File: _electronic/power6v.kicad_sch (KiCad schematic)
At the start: 19 parts

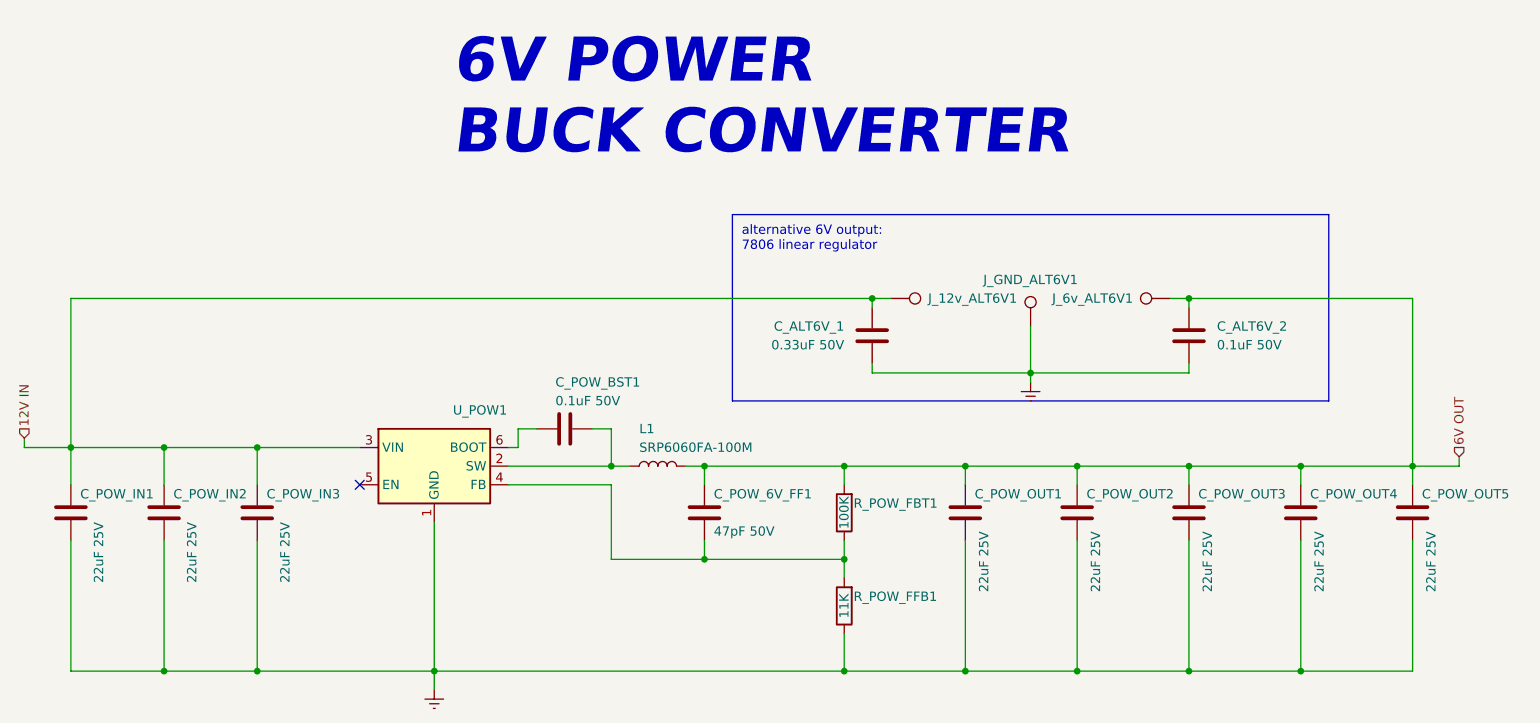
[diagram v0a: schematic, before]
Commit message: BETA first upload
nothing major done here:
* updated KiCAD files to v9
* removed alternative 6v feed-in. The proposed buck converter is fine.
* added to all components LCSC component IDs. With this, exporting the project as gerber files also automatically creates correct BOM for JLCPCB manufacturing
*
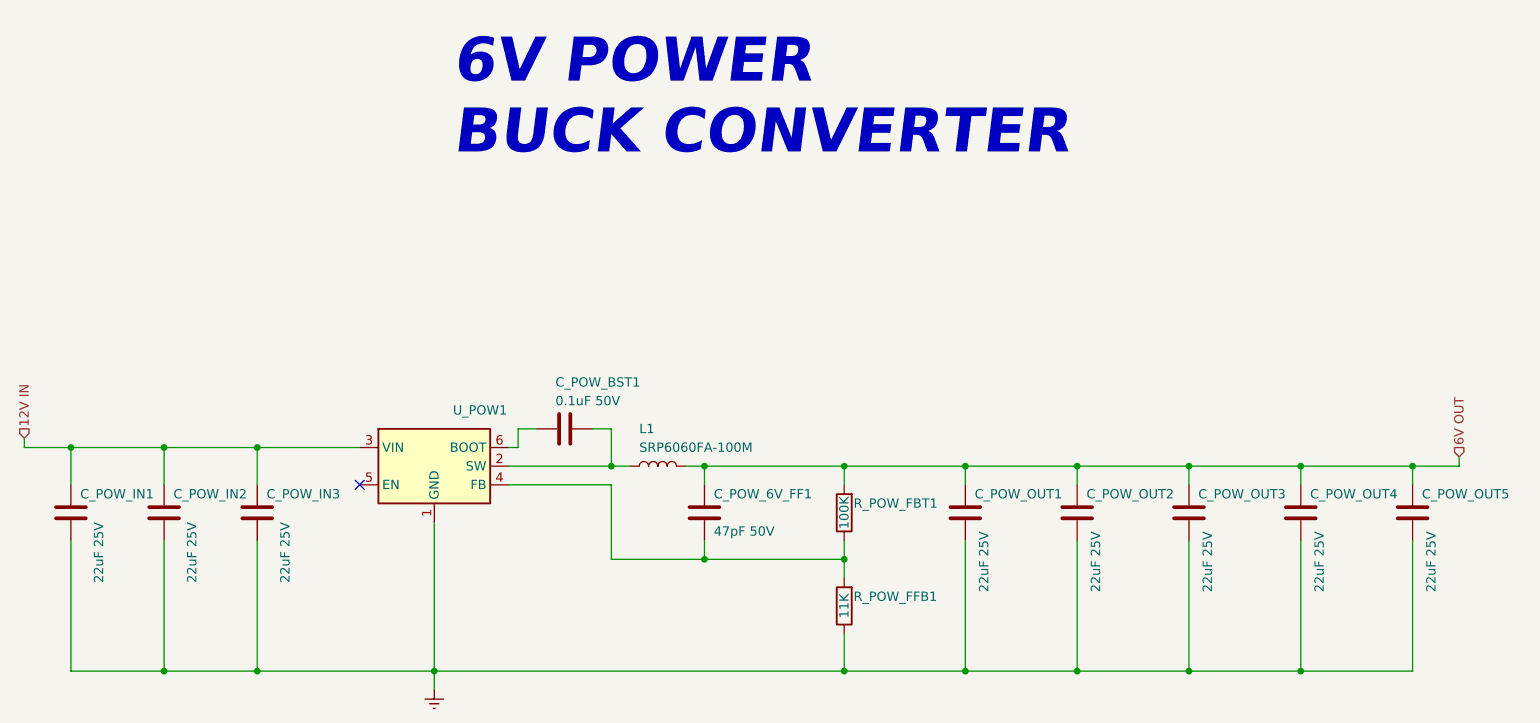
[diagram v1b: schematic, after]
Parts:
- removed C_ALT6V_1: 0.33uF 50V, Capacitor_SMD:C_0603_1608Metric_Pad1.08x0.95mm_HandSolder, symbol Device:C
- removed C_ALT6V_2: 0.1uF 50V, Capacitor_SMD:C_0603_1608Metric_Pad1.08x0.95mm_HandSolder, symbol Device:C
- removed J_12v_ALT6V1, J_6v_ALT6V1, J_GND_ALT6V1: TestPoint, TestPoint:TestPoint_Pad_D1.5mm, symbol Connector:TestPoint
- C_POW_6V_FF1: LCSC (none) -> C1671
- C_POW_BST1: LCSC (none) -> C14663
- C_POW_IN1, C_POW_IN2, C_POW_IN3, C_POW_OUT1, C_POW_OUT2, C_POW_OUT3, C_POW_OUT4, C_POW_OUT5: LCSC (none) -> C52306
- L1: LCSC (none) -> C2046759
- U_POW1: LCSC (none) -> C311983
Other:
- note removed: "alternative 6V output: 7806 linear regulator"
- title: E-TKT v1.0 -> E-TKT v2.0 BETA

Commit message: Added CAD, cleaned up KiCAD some more
Added a FreeCAD Assembly. This will serve for minor updated to the printable parts.
Updated USB-C component to standard KiCAD libary-integrated version, because the pinout of the schematic symbol was messing with the pinout of the footprint
exported the PCB as step so it could be imported to FreeCAD
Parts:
- L1: footprint SRP6060FA:SRP6060FA-4R7M -> EASYEDA2KICAD:IND-SMD_L8.5-W8.0_PSPMAA0803H-330M-ANP; LCSC C2046759 -> C3036141
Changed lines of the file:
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@@
 			)
 		)
-		(property "Footprint" "SRP6060FA:SRP6060FA-4R7M"
+		(property "Footprint" "EASYEDA2KICAD:IND-SMD_L8.5-W8.0_PSPMAA0803H-330M-ANP"
 			(at 138.43 96.52 0)
 			(effects
@@
 			)
 		)
-		(property "LCSC" "C2046759"
+		(property "LCSC" "C3036141"
 			(at 138.43 96.52 90)
 			(effects

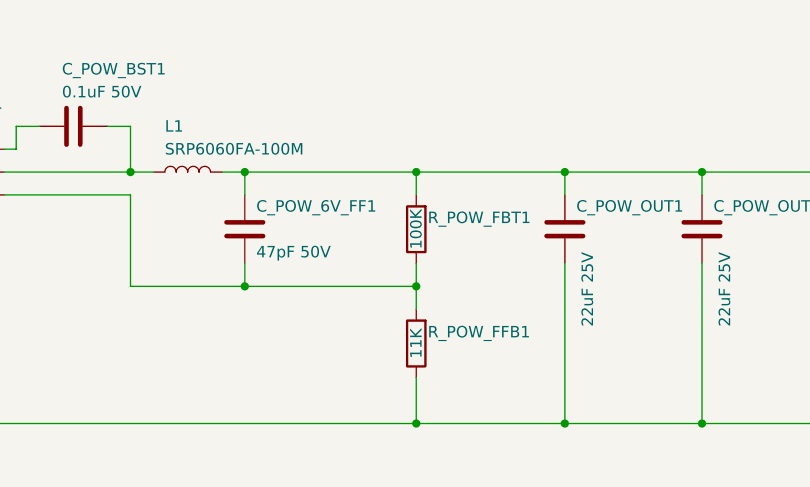
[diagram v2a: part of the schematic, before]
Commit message: JLC export added, LCSC numbers updated
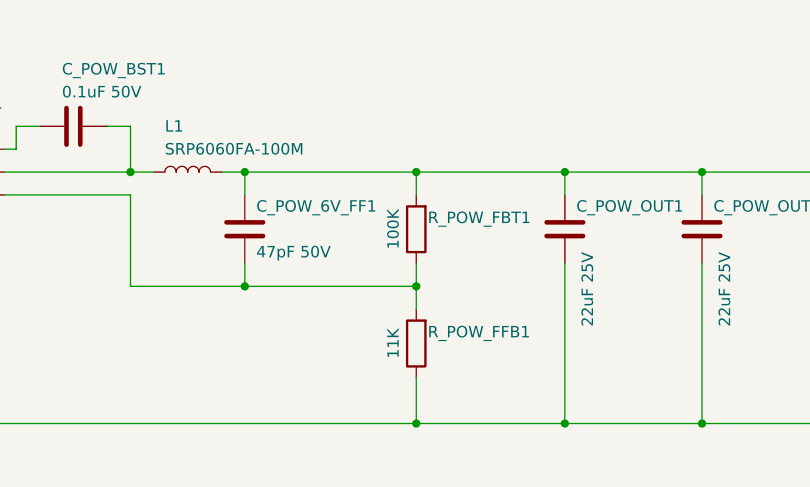
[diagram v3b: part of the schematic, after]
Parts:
- R_POW_FBT1, R_POW_FFB1: LCSC (none) -> C25803
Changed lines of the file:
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@@
 		)
 		(property "Value" "100K"
-			(at 163.83 102.87 90)
+			(at 161.29 102.87 90)
 			(effects
 				(font
@@
 		)
 		(property "Mouser" "OK"
+			(at 163.83 102.87 0)
+			(effects
+				(font
+					(size 1.27 1.27)
+				)
+				(hide yes)
+			)
+		)
+		(property "LCSC" "C25803"
 			(at 163.83 102.87 0)
 			(effects
@@
 		)
 		(property "Value" "11K"
-			(at 163.83 115.57 90)
+			(at 161.29 115.57 90)
 			(effects
 				(font
@@
 			(at 163.83 115.57 0)
 			(effects
+				(font
+					(size 1.27 1.27)
+				)
+				(hide yes)
+			)
+		)
+		(property "LCSC" "C25803"
+			(at 163.83 115.57 0)
+			(effects
